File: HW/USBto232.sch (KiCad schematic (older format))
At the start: 16 parts, among them J1 USB_B_Micro, Q1 Q_NPN_BEC, Q2 Q_NPN_BEC, U2 CP2102N-A01-GQFN28

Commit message: repair mistakes
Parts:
- C22: value 4u7 -> 10u; LCSC C23733 -> C15525
- Q1, Q2: LCSC C20526 -> C20526
- R6: value 2k -> 10k; LCSC C4109 -> C25744
- R8, R9: value 47k -> 10k; LCSC C25792 -> C25744
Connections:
- net GND: no longer J1.6 (Shield)
- net RX_ESP: no longer R9.2
- net TX_ESP: no longer R8.2
- net at U2.18 (~RXT~/GPIO.1): now also R9.2
- net at U2.19 (~TXT~/GPIO.0): now also R8.2
- no-connect marks 3 -> 4
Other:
- moved on the sheet: D10, D11, R8, R9
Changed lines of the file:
@@
 Comment4 ""
 $EndDescr
-Text HLabel 7350 2100 2    50   Input ~ 0
-TX_ESP
-Text HLabel 7350 2300 2    50   Input ~ 0
+Text HLabel 6700 2300 1    50   Input ~ 0
 RX_ESP
 $Comp
@@
 P 4500 2500
 F 0 "R6" H 4570 2546 50  0000 L CNN
-F 1 "2k" H 4570 2455 50  0000 L CNN
+F 1 "10k" H 4570 2455 50  0000 L CNN
 F 2 "Resistor_SMD:R_0402_1005Metric" V 4430 2500 50  0001 C CNN
 F 3 "~" H 4500 2500 50  0001 C CNN
-F 4 "C4109" H 4500 2500 50  0001 C CNN "LCSC"
+F 4 "C25744" H 4500 2500 50  0001 C CNN "LCSC"
 F 5 "0;0;0" H 4500 2500 50  0001 C CNN "JLCPCB_CORRECTION"
 	1    4500 2500
@@
 L Device:R R8
 U 1 1 5F7740AD
-P 6550 2350
-F 0 "R8" H 6620 2396 50  0000 L CNN
-F 1 "47k" H 6620 2305 50  0000 L CNN
-F 2 "Resistor_SMD:R_0402_1005Metric" V 6480 2350 50  0001 C CNN
-F 3 "~" H 6550 2350 50  0001 C CNN
-F 4 "C25792" H 6550 2350 50  0001 C CNN "LCSC"
-F 5 "0;0;0" H 6550 2350 50  0001 C CNN "JLCPCB_CORRECTION"
-	1    6550 2350
-	1    0    0    -1
+P 6300 4200
+F 0 "R8" V 6200 4050 50  0000 L CNN
+F 1 "10k" V 6200 4250 50  0000 L CNN
+F 2 "Resistor_SMD:R_0402_1005Metric" V 6230 4200 50  0001 C CNN
+F 3 "~" H 6300 4200 50  0001 C CNN
+F 4 "C25744" H 6300 4200 50  0001 C CNN "LCSC"
+F 5 "0;0;0" H 6300 4200 50  0001 C CNN "JLCPCB_CORRECTION"
+	1    6300 4200
+	0    1    1    0
 $EndComp
 $Comp
 L Device:R R9
 U 1 1 5F774323
-P 6850 2350
-F 0 "R9" H 6920 2396 50  0000 L CNN
-F 1 "47k" H 6920 2305 50  0000 L CNN
-F 2 "Resistor_SMD:R_0402_1005Metric" V 6780 2350 50  0001 C CNN
-F 3 "~" H 6850 2350 50  0001 C CNN
-F 4 "C25792" H 6850 2350 50  0001 C CNN "LCSC"
-F 5 "0;0;0" H 6850 2350 50  0001 C CNN "JLCPCB_CORRECTION"
-	1    6850 2350
-	1    0    0    -1
+P 6300 4300
+F 0 "R9" V 6400 4150 50  0000 L CNN
+F 1 "10k" V 6400 4350 50  0000 L CNN
+F 2 "Resistor_SMD:R_0402_1005Metric" V 6230 4300 50  0001 C CNN
+F 3 "~" H 6300 4300 50  0001 C CNN
+F 4 "C25744" H 6300 4300 50  0001 C CNN "LCSC"
+F 5 "0;0;0" H 6300 4300 50  0001 C CNN "JLCPCB_CORRECTION"
+	1    6300 4300
+	0    1    1    0
 $EndComp
 $Comp
 L Device:LED D10
 U 1 1 5F774688
-P 6550 1950
-F 0 "D10" V 6550 2150 50  0000 R CNN
-F 1 "green" V 6650 2200 50  0000 R CNN
-F 2 "LED_SMD:LED_0603_1608Metric" H 6550 1950 50  0001 C CNN
-F 3 "~" H 6550 1950 50  0001 C CNN
-F 4 "C72043" H 6550 1950 50  0001 C CNN "LCSC"
-F 5 "0;0;0" H 6550 1950 50  0001 C CNN "JLCPCB_CORRECTION"
-	1    6550 1950
-	0    -1   -1   0
+P 7050 4200
+F 0 "D10" H 7050 4300 50  0000 R CNN
+F 1 "green" H 7300 4300 50  0000 R CNN
+F 2 "LED_SMD:LED_0603_1608Metric" H 7050 4200 50  0001 C CNN
+F 3 "~" H 7050 4200 50  0001 C CNN
+F 4 "C72043" H 7050 4200 50  0001 C CNN "LCSC"
+F 5 "0;0;0" H 7050 4200 50  0001 C CNN "JLCPCB_CORRECTION"
+	1    7050 4200
+	1    0    0    -1
 $EndComp
 $Comp
 L Device:LED D11
 U 1 1 5F774C1B
-P 6850 1950
-F 0 "D11" V 6800 2000 50  0000 L CNN
-F 1 "green" V 6950 2000 50  0000 L CNN
-F 2 "LED_SMD:LED_0603_1608Metric" H 6850 1950 50  0001 C CNN
-F 3 "~" H 6850 1950 50  0001 C CNN
-F 4 "C72043" H 6850 1950 50  0001 C CNN "LCSC"
-F 5 "0;0;0" H 6850 1950 50  0001 C CNN "JLCPCB_CORRECTION"
-	1    6850 1950
-	0    -1   -1   0
-$EndComp
-Wire Wire Line
-	6550 1650 6550 1800
-Wire Wire Line
-	6850 1650 6850 1800
-Wire Wire Line
-	6550 2100 6550 2200
-Wire Wire Line
-	6850 2100 6850 2200
+P 6700 4300
+F 0 "D11" H 6600 4150 50  0000 L CNN
+F 1 "green" H 6750 4200 50  0000 L CNN
+F 2 "LED_SMD:LED_0603_1608Metric" H 6700 4300 50  0001 C CNN
+F 3 "~" H 6700 4300 50  0001 C CNN
+F 4 "C72043" H 6700 4300 50  0001 C CNN "LCSC"
+F 5 "0;0;0" H 6700 4300 50  0001 C CNN "JLCPCB_CORRECTION"
+	1    6700 4300
+	1    0    0    -1
+$EndComp
+Wire Wire Line
+	7350 4200 7200 4200
+Wire Wire Line
+	7350 4300 6850 4300
+Wire Wire Line
+	6900 4200 6450 4200
+Wire Wire Line
+	6550 4300 6450 4300
 $Comp
 L Interface_USB:CP2102N-A01-GQFN28 U2
@@
 	5400 2250 5400 2400
 Wire Wire Line
-	6000 2800 6550 2800
-Wire Wire Line
-	6000 2900 6850 2900
-Wire Wire Line
-	6850 2500 6850 2900
+	6150 4300 6000 4300
 NoConn ~ 6000 3600
 NoConn ~ 6000 3500
@@
 F 2 "Package_TO_SOT_SMD:SOT-23" H 8250 2800 50  0001 C CNN
 F 3 "~" H 8050 2700 50  0001 C CNN
-F 4 " C20526" H 8050 2700 50  0001 C CNN "LCSC"
+F 4 "C20526" H 8050 2700 50  0001 C CNN "LCSC"
 F 5 "0;0;180" H 8050 2700 50  0001 C CNN "JLCPCB_CORRECTION"
 	1    8050 2700
@@
 F 2 "Package_TO_SOT_SMD:SOT-23" H 7450 3200 50  0001 C CNN
 F 3 "~" H 7250 3100 50  0001 C CNN
-F 4 " C20526" H 7250 3100 50  0001 C CNN "LCSC"
+F 4 "C20526" H 7250 3100 50  0001 C CNN "LCSC"
 F 5 "0;0;180" H 7250 3100 50  0001 C CNN "JLCPCB_CORRECTION"
 	1    7250 3100
@@
 L power:+3V3 #PWR041
 U 1 1 5FAFF359
-P 6550 1650
-F 0 "#PWR041" H 6550 1500 50  0001 C CNN
-F 1 "+3V3" H 6565 1823 50  0000 C CNN
-F 2 "" H 6550 1650 50  0001 C CNN
-F 3 "" H 6550 1650 50  0001 C CNN
-	1    6550 1650
-	1    0    0    -1
+P 7350 4200
+F 0 "#PWR041" H 7350 4050 50  0001 C CNN
+F 1 "+3V3" V 7250 4300 50  0000 C CNN
+F 2 "" H 7350 4200 50  0001 C CNN
+F 3 "" H 7350 4200 50  0001 C CNN
+	1    7350 4200
+	0    1    1    0
 $EndComp
 $Comp
 L power:+3V3 #PWR042
 U 1 1 5FAFF4D0
-P 6850 1650
-F 0 "#PWR042" H 6850 1500 50  0001 C CNN
-F 1 "+3V3" H 6865 1823 50  0000 C CNN
-F 2 "" H 6850 1650 50  0001 C CNN
-F 3 "" H 6850 1650 50  0001 C CNN
-	1    6850 1650
-	1    0    0    -1
+P 7350 4300
+F 0 "#PWR042" H 7350 4150 50  0001 C CNN
+F 1 "+3V3" V 7450 4400 50  0000 C CNN
+F 2 "" H 7350 4300 50  0001 C CNN
+F 3 "" H 7350 4300 50  0001 C CNN
+	1    7350 4300
+	0    1    1    0
 $EndComp
 Wire Wire Line
@@
 P 5900 1950
 F 0 "C22" V 5648 1950 50  0000 C CNN
-F 1 "4u7" V 5739 1950 50  0000 C CNN
+F 1 "10u" V 5739 1950 50  0000 C CNN
 F 2 "Capacitor_SMD:C_0402_1005Metric" H 5938 1800 50  0001 C CNN
 F 3 "~" H 5900 1950 50  0001 C CNN
-F 4 "C23733" H 5900 1950 50  0001 C CNN "LCSC"
+F 4 "C15525" H 5900 1950 50  0001 C CNN "LCSC"
 F 5 "0;0;0" H 5900 1950 50  0001 C CNN "JLCPCB_CORRECTION"
 	1    5900 1950
@@
 $EndComp
 Wire Wire Line
-	7350 2100 7150 2100
-Wire Wire Line
-	7350 2300 7250 2300
-Wire Wire Line
-	7250 2300 7250 2900
-Wire Wire Line
-	7250 2900 6850 2900
-Connection ~ 6850 2900
-Wire Wire Line
-	6550 2800 7150 2800
-Connection ~ 6550 2800
-Wire Wire Line
-	7150 2100 7150 2800
-Wire Wire Line
-	6550 2500 6550 2800
+	6700 2300 6700 2900
 $Comp
 L power:+5V #PWR037
@@
 Wire Wire Line
 	3800 3100 3600 3100
-$Comp
-L power:GND #PWR031
-U 1 1 5FB5E49D
-P 3200 3500
-AR Path="/5FBB3550/5FB5E49D" Ref="#PWR031"  Part="1"
-AR Path="/5FB5E49D" Ref="#PWR?"  Part="1"
-AR Path="/5F78DB3E/5FB5E49D" Ref="#PWR?"  Part="1"
-F 0 "#PWR031" H 3200 3250 50  0001 C CNN
-F 1 "GND" H 3050 3450 50  0000 C CNN
-F 2 "" H 3200 3500 50  0001 C CNN
-F 3 "" H 3200 3500 50  0001 C CNN
-	1    3200 3500
-	1    0    0    -1
-$EndComp
 NoConn ~ 3600 3300
 Wire Wire Line
@@
 Text HLabel 3950 2750 1    50   Input ~ 0
 V_OUT
+NoConn ~ 3200 3500
+Wire Wire Line
+	6000 2800 6550 2800
+Wire Wire Line
+	6000 2900 6700 2900
+Wire Wire Line
+	6550 2300 6550 2800
+Text HLabel 6550 2300 1    50   Input ~ 0
+TX_ESP
+Wire Wire Line
+	6000 4200 6150 4200
 $EndSCHEMATC

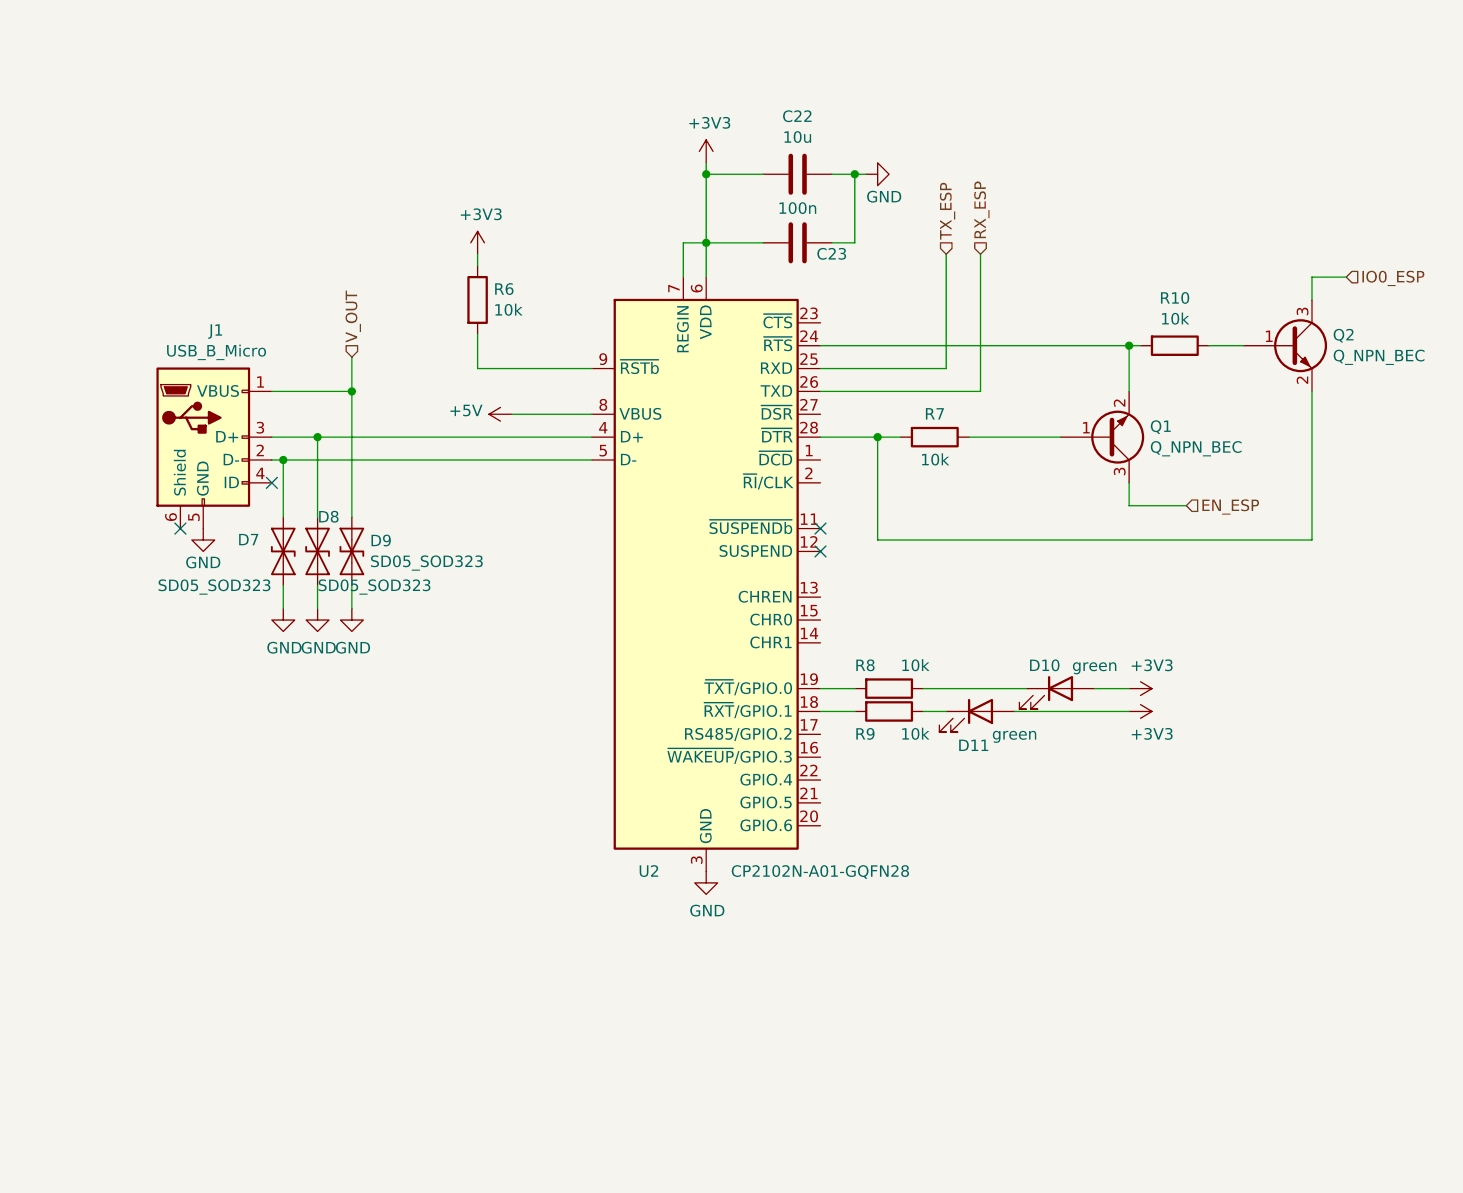
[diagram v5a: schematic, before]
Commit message: repair footprint of DIP and USB micro, change buttons with higher fretboard
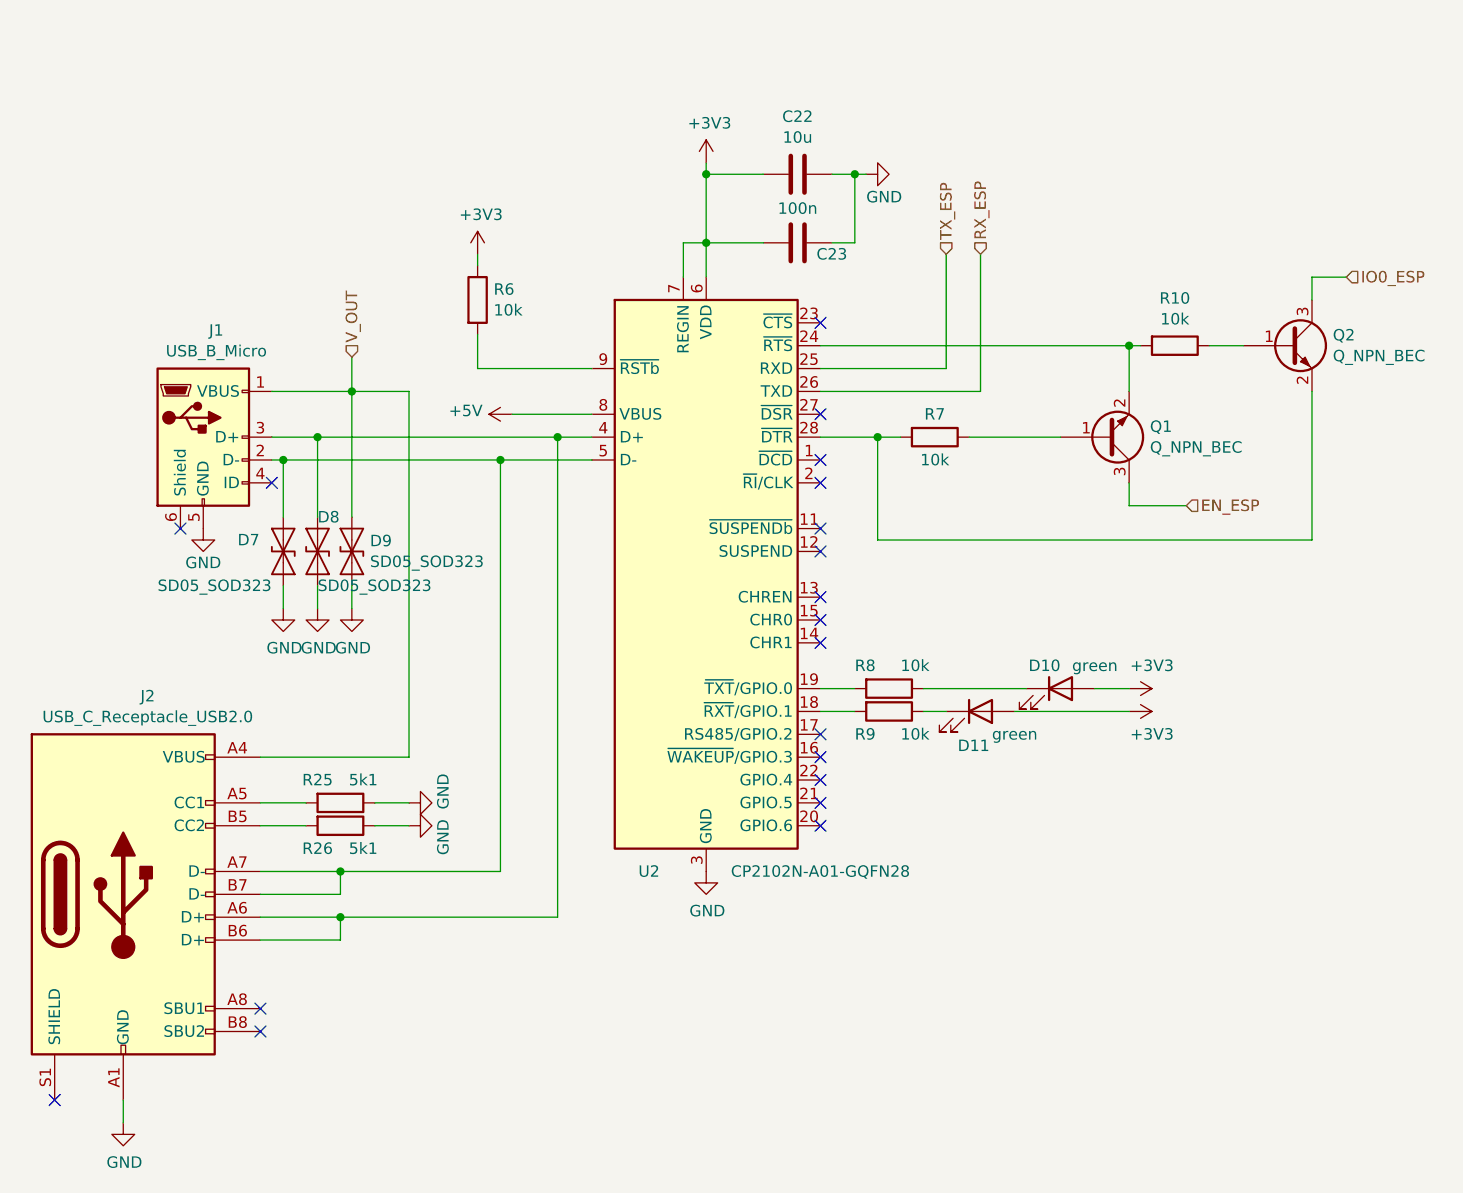
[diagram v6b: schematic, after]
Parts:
- added J2: USB_C_Receptacle_USB2.0, Connector_USB:USB_C_Receptacle_HRO_TYPE-C-31-M-12, symbol Connector:USB_C_Receptacle_USB2.0
- added R25, R26: 5k1, Resistor_SMD:R_0402_1005Metric, symbol Device:R
- J1: footprint Connector_USB:USB_Micro-B_Wuerth_629105150521 -> my_library:USB_micro_JLCPCB_con
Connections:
- net GND: now also J2.A1 (GND), J2.A12 (GND), J2.B1 (GND), J2.B12 (GND), R25.1, R26.1
- net V_OUT: now also J2.A4 (VBUS), J2.A9 (VBUS), J2.B4 (VBUS), J2.B9 (VBUS)
- net at D8.2 (A2), J1.3 (D+), U2.4 (D+): now also J2.A6 (D+), J2.B6 (D+)
- net at D7.2 (A2), J1.2 (D-), U2.5 (D-): now also J2.A7 (D-), J2.B7 (D-)
- new net: J2.A5 (CC1), R25.2
- new net: J2.B5 (CC2), R26.2
- no-connect marks 4 -> 19
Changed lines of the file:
@@
 F 0 "J1" H 3357 3567 50  0000 C CNN
 F 1 "USB_B_Micro" H 3357 3476 50  0000 C CNN
-F 2 "Connector_USB:USB_Micro-B_Wuerth_629105150521" H 3450 3050 50  0001 C CNN
+F 2 "my_library:USB_micro_JLCPCB_con" H 3450 3050 50  0001 C CNN
 F 3 "~" H 3450 3050 50  0001 C CNN
 F 4 "ručně" H 3300 3100 50  0001 C CNN "LCSC"
@@
 	3950 2750 3950 2900
 Wire Wire Line
-	3800 3100 5000 3100
-Wire Wire Line
-	3650 3200 5000 3200
+	3800 3100 4850 3100
+Wire Wire Line
+	3650 3200 4600 3200
 Text HLabel 3950 2750 1    50   Input ~ 0
 V_OUT
@@
 Wire Wire Line
 	6000 4200 6150 4200
+$Comp
+L Connector:USB_C_Receptacle_USB2.0 J2
+U 1 1 604A6679
+P 2950 5100
+F 0 "J2" H 3057 5967 50  0000 C CNN
+F 1 "USB_C_Receptacle_USB2.0" H 3057 5876 50  0000 C CNN
+F 2 "Connector_USB:USB_C_Receptacle_HRO_TYPE-C-31-M-12" H 3100 5100 50  0001 C CNN
+F 3 "https://www.usb.org/sites/default/files/documents/usb_type-c.zip" H 3100 5100 50  0001 C CNN
+F 4 "0;0;0" H 2950 5100 50  0001 C CNN "JLCPCB_CORRECTION"
+F 5 "C165948" H 2950 5100 50  0001 C CNN "LCSC"
+	1    2950 5100
+	1    0    0    -1
+$EndComp
+Wire Wire Line
+	3550 4500 4200 4500
+Wire Wire Line
+	4200 4500 4200 2900
+Wire Wire Line
+	4200 2900 3950 2900
+Wire Wire Line
+	3550 5000 3900 5000
+Wire Wire Line
+	4600 5000 4600 3200
+Connection ~ 4600 3200
+Wire Wire Line
+	4600 3200 5000 3200
+Wire Wire Line
+	3550 5200 3900 5200
+Wire Wire Line
+	4850 5200 4850 3100
+Connection ~ 4850 3100
+Wire Wire Line
+	4850 3100 5000 3100
+Wire Wire Line
+	3550 5100 3900 5100
+Wire Wire Line
+	3900 5100 3900 5000
+Connection ~ 3900 5000
+Wire Wire Line
+	3900 5000 4600 5000
+Wire Wire Line
+	3550 5300 3900 5300
+Wire Wire Line
+	3900 5300 3900 5200
+Connection ~ 3900 5200
+Wire Wire Line
+	3900 5200 4850 5200
+$Comp
+L power:GND #PWR0226
+U 1 1 604B0E91
+P 2950 6100
+AR Path="/5FBB3550/604B0E91" Ref="#PWR0226"  Part="1"
+AR Path="/604B0E91" Ref="#PWR?"  Part="1"
+AR Path="/5F78DB3E/604B0E91" Ref="#PWR?"  Part="1"
+F 0 "#PWR0226" H 2950 5850 50  0001 C CNN
+F 1 "GND" H 2955 5927 50  0000 C CNN
+F 2 "" H 2950 6100 50  0001 C CNN
+F 3 "" H 2950 6100 50  0001 C CNN
+	1    2950 6100
+	1    0    0    -1
+$EndComp
+Wire Wire Line
+	2950 6100 2950 6000
+NoConn ~ 2650 6000
+$Comp
+L Device:R R25
+U 1 1 604B4A7E
+P 3900 4700
+F 0 "R25" V 3800 4600 50  0000 C CNN
+F 1 "5k1" V 3800 4800 50  0000 C CNN
+F 2 "Resistor_SMD:R_0402_1005Metric" V 3830 4700 50  0001 C CNN
+F 3 "~" H 3900 4700 50  0001 C CNN
+F 4 "0;0;0" H 3900 4700 50  0001 C CNN "JLCPCB_CORRECTION"
+F 5 "C25905" H 3900 4700 50  0001 C CNN "LCSC"
+	1    3900 4700
+	0    1    1    0
+$EndComp
+$Comp
+L Device:R R26
+U 1 1 604B4F88
+P 3900 4800
+F 0 "R26" V 4000 4700 50  0000 C CNN
+F 1 "5k1" V 4000 4900 50  0000 C CNN
+F 2 "Resistor_SMD:R_0402_1005Metric" V 3830 4800 50  0001 C CNN
+F 3 "~" H 3900 4800 50  0001 C CNN
+F 4 "0;0;0" H 3900 4800 50  0001 C CNN "JLCPCB_CORRECTION"
+F 5 "C25905" H 3900 4800 50  0001 C CNN "LCSC"
+	1    3900 4800
+	0    1    1    0
+$EndComp
+$Comp
+L power:GND #PWR0227
+U 1 1 604B514C
+P 4200 4700
+AR Path="/5FBB3550/604B514C" Ref="#PWR0227"  Part="1"
+AR Path="/604B514C" Ref="#PWR?"  Part="1"
+AR Path="/5F78DB3E/604B514C" Ref="#PWR?"  Part="1"
+F 0 "#PWR0227" H 4200 4450 50  0001 C CNN
+F 1 "GND" H 4250 4550 50  0000 C CNN
+F 2 "" H 4200 4700 50  0001 C CNN
+F 3 "" H 4200 4700 50  0001 C CNN
+	1    4200 4700
+	0    -1   -1   0
+$EndComp
+$Comp
+L power:GND #PWR0228
+U 1 1 604B5736
+P 4200 4800
+AR Path="/5FBB3550/604B5736" Ref="#PWR0228"  Part="1"
+AR Path="/604B5736" Ref="#PWR?"  Part="1"
+AR Path="/5F78DB3E/604B5736" Ref="#PWR?"  Part="1"
+F 0 "#PWR0228" H 4200 4550 50  0001 C CNN
+F 1 "GND" H 4150 4650 50  0000 C CNN
+F 2 "" H 4200 4800 50  0001 C CNN
+F 3 "" H 4200 4800 50  0001 C CNN
+	1    4200 4800
+	0    -1   -1   0
+$EndComp
+Wire Wire Line
+	3750 4700 3550 4700
+Wire Wire Line
+	3550 4800 3750 4800
+Wire Wire Line
+	4050 4800 4200 4800
+Wire Wire Line
+	4200 4700 4050 4700
+NoConn ~ 6000 2600
+NoConn ~ 6000 3000
+NoConn ~ 6000 3200
+NoConn ~ 6000 3300
+NoConn ~ 6000 3800
+NoConn ~ 6000 3900
+NoConn ~ 6000 4000
+NoConn ~ 6000 4400
+NoConn ~ 6000 4500
+NoConn ~ 6000 4600
+NoConn ~ 6000 4700
+NoConn ~ 6000 4800
+NoConn ~ 3550 5600
+NoConn ~ 3550 5700
 $EndSCHEMATC

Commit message: change USB footprint, add 3. DIP
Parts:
- J1: LCSC ručně -> C319164
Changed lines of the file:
@@
 F 2 "my_library:USB_micro_JLCPCB_con" H 3450 3050 50  0001 C CNN
 F 3 "~" H 3450 3050 50  0001 C CNN
-F 4 "ručně" H 3300 3100 50  0001 C CNN "LCSC"
+F 4 "C319164" H 3300 3100 50  0001 C CNN "LCSC"
 F 5 "0;0;0" H 3300 3100 50  0001 C CNN "JLCPCB_CORRECTION"
 	1    3300 3100

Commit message: update rotation of components for fab, update folder fab
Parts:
- J2: JLCPCB_CORRECTION 0;0;0 -> 0;0;180
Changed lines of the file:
@@
 F 2 "Connector_USB:USB_C_Receptacle_HRO_TYPE-C-31-M-12" H 3100 5100 50  0001 C CNN
 F 3 "https://www.usb.org/sites/default/files/documents/usb_type-c.zip" H 3100 5100 50  0001 C CNN
-F 4 "0;0;0" H 2950 5100 50  0001 C CNN "JLCPCB_CORRECTION"
+F 4 "0;0;180" H 2950 5100 50  0001 C CNN "JLCPCB_CORRECTION"
 F 5 "C165948" H 2950 5100 50  0001 C CNN "LCSC"
 	1    2950 5100
